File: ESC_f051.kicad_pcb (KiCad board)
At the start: 2 copper layers, 25.7 x 24.1 mm, 56 parts, among them Q1 2N7002, Q2 2N7002, Q3 2N7002, Q4 AO4407A, Q5 AO4406A, Q6 AO4407A, Q7 AO4406A, Q8 AO4407A, Q9 AO4406A, U1 XC6206PxxxMR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

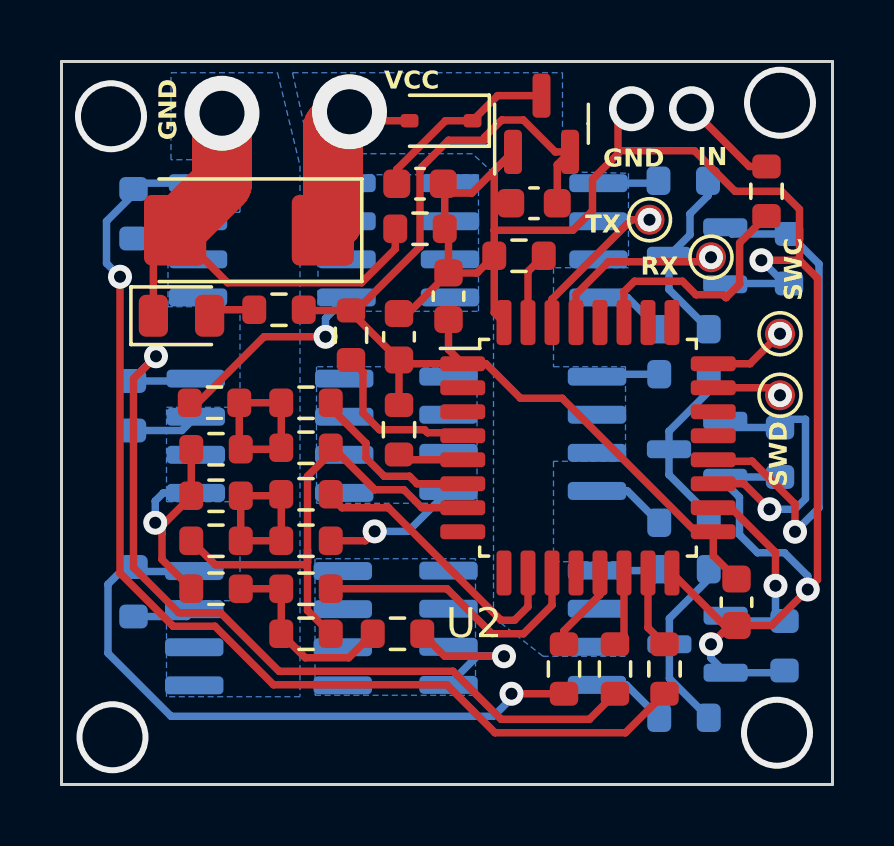
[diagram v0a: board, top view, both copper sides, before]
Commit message: reduced the size
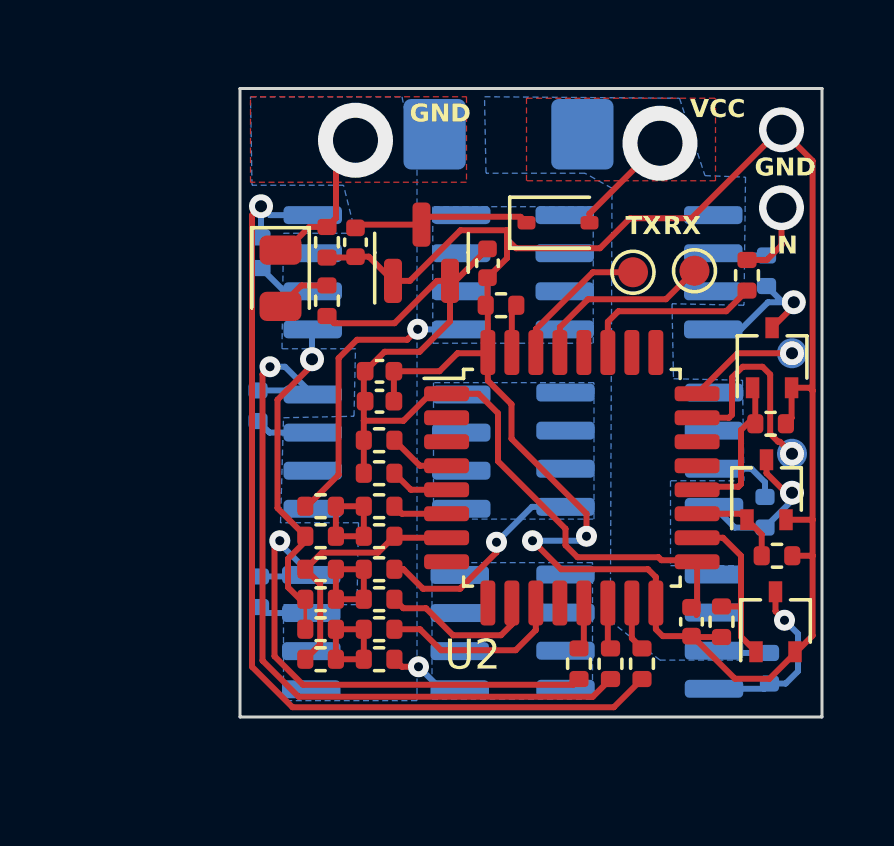
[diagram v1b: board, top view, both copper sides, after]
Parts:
- removed R23, R26, R29: 100, Resistor_SMD:R_0603_1608Metric
- C1, TP5, TP6: moved to B.Cu
- C2, C3, C4, C5, C6: footprint Capacitor_SMD:C_0603_1608Metric -> Capacitor_SMD:C_0402_1005Metric
- Q1, Q2, Q3: value 2N7002 -> BSS214NW; footprint Package_TO_SOT_SMD:SOT-23 -> Package_TO_SOT_SMD:SOT-323_SC-70; moved to F.Cu
- R1, R10, R11, R12, R13, R14, R15, R16, R17, R18, R2, R24, R27, R3, R30, R31, R32, R33, R4, R5, R6, R7, R8: footprint Resistor_SMD:R_0603_1608Metric -> Resistor_SMD:R_0402_1005Metric
- R19, R20, R21: footprint Resistor_SMD:R_0603_1608Metric -> Resistor_SMD:R_0402_1005Metric; moved to F.Cu
- R22, R25, R28: value 1k -> 470; footprint Resistor_SMD:R_0603_1608Metric -> Resistor_SMD:R_0402_1005Metric
- R9: value 10K -> 10k; footprint Resistor_SMD:R_0603_1608Metric -> Resistor_SMD:R_0402_1005Metric
- moved C1 9.22 mm to (154.7, 57.0)
- moved U1 5.87 mm to (151.8, 61.0)
- moved R19 5.53 mm to (163.4, 66.7), turned to 180 degrees
- moved R25 5.33 mm to (163.2, 69.7), turned to 90 degrees
- moved D1 5.17 mm to (156.3, 60.0), turned to 0 degrees
- moved R14 4.94 mm to (148.4, 69.5)
- moved R13 4.90 mm to (148.4, 72.5)
- moved R15 4.53 mm to (148.4, 70.5)
- moved R31 4.44 mm to (146.4, 61.0)
- moved R28 4.36 mm to (163.4, 74.8), turned to 90 degrees
- moved R5 4.26 mm to (150.4, 72.5)
- moved R7 4.22 mm to (150.4, 69.5)
- moved Q1 4.22 mm to (163.5, 64.5), turned to 90 degrees
- moved R33 4.20 mm to (146.4, 72.3)
- moved R32 4.20 mm to (146.3, 66.1)
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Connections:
- Q4 pad 4: Net-(Q4-G) -> Net-(Q1-D)
- Q6 pad 4: Net-(Q6-G) -> Net-(Q2-D)
- Q8 pad 4: Net-(Q8-G) -> Net-(Q3-D)
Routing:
- net /OUT_A1: track 17.1 -> 5.09 mm, vias 1 -> 0
- net GND: track 31.8 -> 22.4 mm
- net /ADC_0: track 16.7 -> 8.60 mm
- net /OUT_B1: track 9.10 -> 3.15 mm, vias 1 -> 0
- net GNDD: track 65.4 -> 71.2 mm, vias 4 -> 3
- net /SYS_SWDIO: track 2.33 -> 6.95 mm
- net Net-(Q9-G): track 22.3 -> 17.9 mm
- net /ADC_B: track 9.67 -> 5.28 mm
- net Net-(Q5-G): track 36.5 -> 32.3 mm
- net /ADC_A: track 5.91 -> 1.84 mm
- net +3.3V: track 35.7 -> 31.6 mm
- net Net-(U2-NRST): track 5.58 -> 2.09 mm
- net /ADC_C: track 9.46 -> 6.18 mm
- net Net-(Q7-G): track 29.2 -> 25.9 mm
- net VCC: track 12.7 -> 9.69 mm
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- added copper zone on F.Cu, net GND
- added copper zone on F.Cu, net VCC
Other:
- board size 25.7 x 24.1 mm -> 19.4 x 20.9 mm
- board text added: "CL"
- board text removed: "SWC"
